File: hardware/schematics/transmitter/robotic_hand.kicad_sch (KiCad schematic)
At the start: 24 parts, among them J1 Conn_01x04_Socket, SW1 SW_BOOT, SW2 SW_RESET, U2 AMS1117-3.3, U3 ESP32-WROOM-32

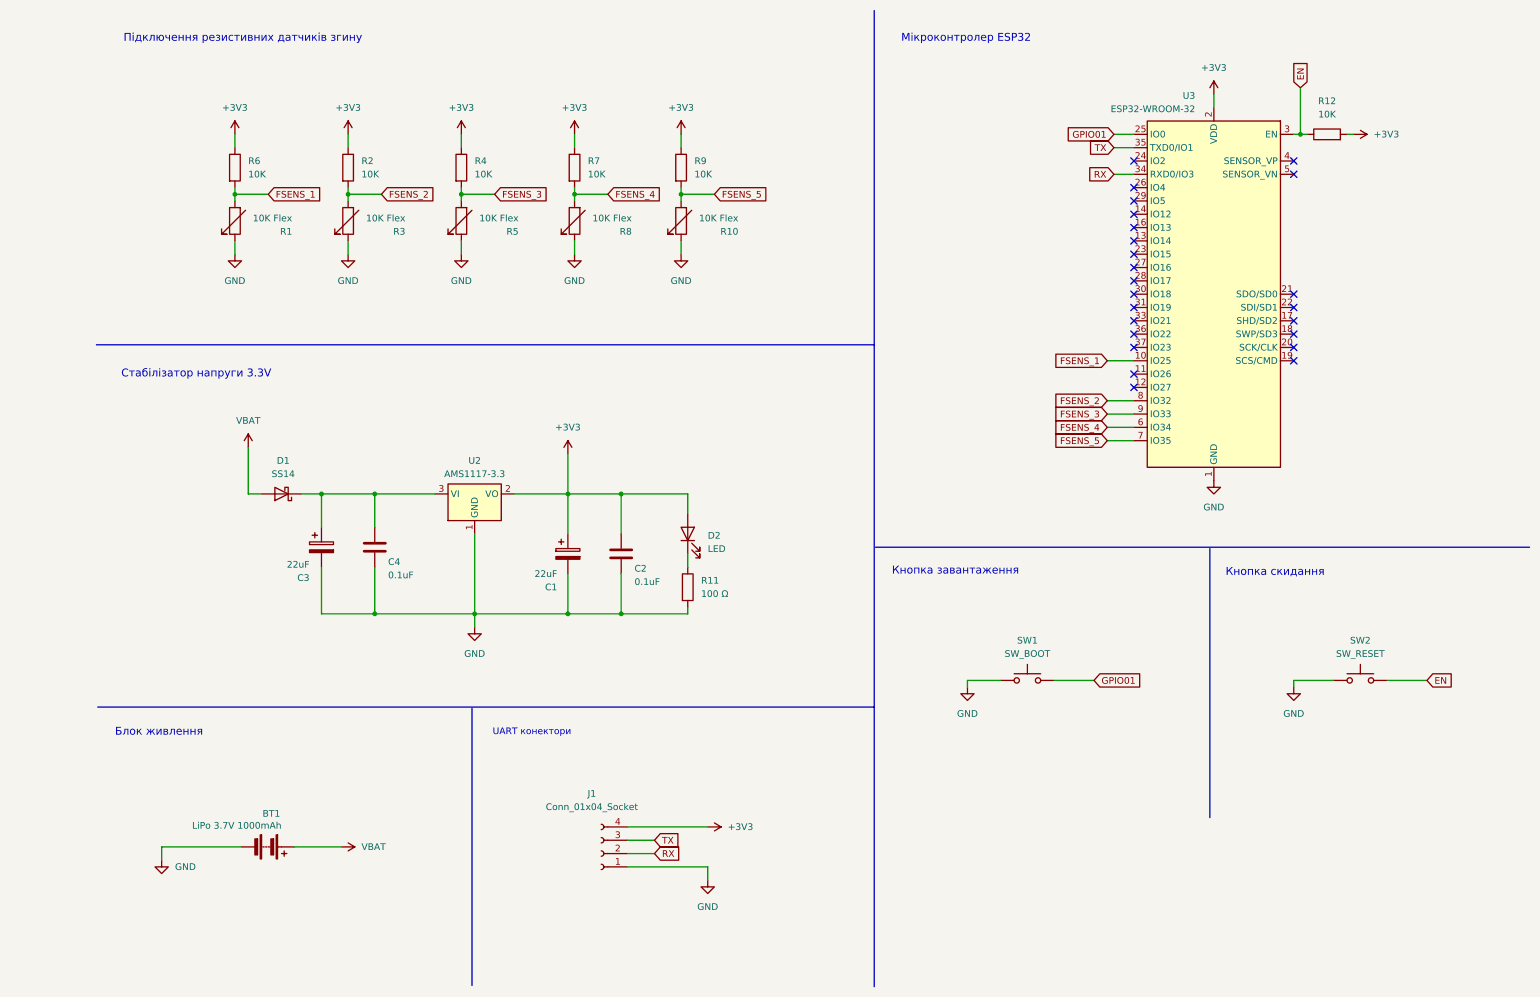
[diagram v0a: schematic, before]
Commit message: Revert schematics to rev-A Arduino design; ESP32 redesign split to separate project
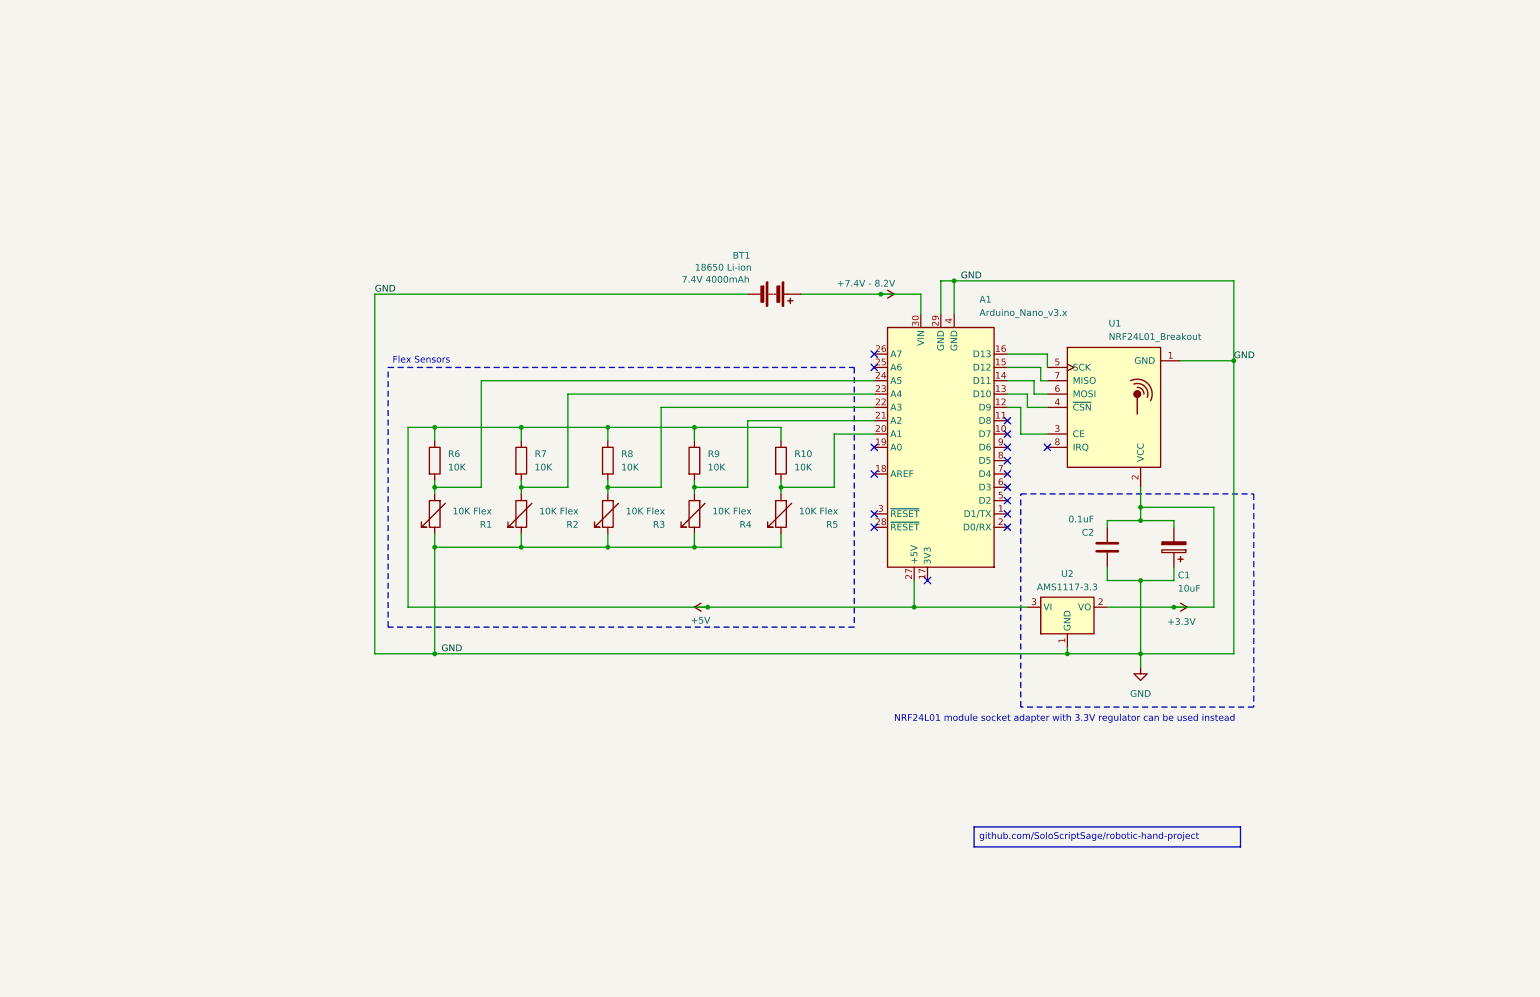
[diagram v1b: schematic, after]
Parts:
- removed C3: 22uF, Capacitor_SMD:C_1206_3216Metric, symbol Device:C_Polarized
- removed C4: 0.1uF, Capacitor_SMD:C_0805_2012Metric, symbol Device:C
- removed D1: SS14, Diode_SMD:D_SMA, symbol Diode:SS14
- removed D2: LED, LED_SMD:LED_0805_2012Metric, symbol Device:LED
- removed J1: Conn_01x04_Socket, Connector_PinHeader_2.54mm:PinHeader_1x04_P2.54mm_Vertical, symbol Connector:Conn_01x04_Socket
- removed R10, R8: 10K Flex, Connector_JST:JST_PH_S2B-PH-K_1x02_P2.00mm_Horizontal, symbol Device:R_Variable
- removed R11: 100 Ω, Resistor_SMD:R_0805_2012Metric, symbol Device:R
- removed R12, R2, R4: 10K, Resistor_SMD:R_0805_2012Metric, symbol Device:R
- removed SW1: SW_BOOT, Button_Switch_SMD:SW_SPST_B3U-1000P, symbol Switch:SW_Push
- removed SW2: SW_RESET, Button_Switch_SMD:SW_SPST_B3U-1000P, symbol Switch:SW_Push
- removed U3: ESP32-WROOM-32, RF_Module:ESP32-WROOM-32, symbol RF_Module:ESP32-WROOM-32
- added A1: Arduino_Nano_v3.x, Module:Arduino_Nano, symbol MCU_Module:Arduino_Nano_v3.x
- added R10, R8: 10K, symbol Device:R
- added R2, R4: 10K Flex, symbol Device:R_Variable
- added U1: NRF24L01_Breakout, RF_Module:nRF24L01_Breakout, symbol RF:NRF24L01_Breakout
- BT1: value LiPo 3.7V 1000mAh -> 18650 Li-ion; footprint Connector_JST:JST_PH_S2B-PH-K_1x02_P2.00mm_Horizontal -> (none)
- C1: value 22uF -> 10uF; footprint Capacitor_SMD:C_1206_3216Metric -> (none)
- C2: footprint Capacitor_SMD:C_0805_2012Metric -> (none)
- R1, R3, R5: footprint Connector_JST:JST_PH_S2B-PH-K_1x02_P2.00mm_Horizontal -> (none)
- R6, R7, R9: footprint Resistor_SMD:R_0805_2012Metric -> (none)
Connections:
- net GND: now also C1.1, C2.2, A1.29 (GND), A1.4 (GND), R2.1, R4.1, U1.1 (GND); no longer C1.2, C2.1
- net +5V: now reaches U2.3 (VI)
- net +5V: now also R6.1, R7.1, R9.1, A1.27 (+5V), R10.1, R8.1
- removed net +3V3: C1.1, C2.2, R6.1, R7.1, R9.1, U2.2 (VO)
- net FSENS_1: no longer names the net of R1.2, R6.2
- net FSENS_1: now also A1.24 (A5)
- net FSENS_2: no longer names the net of R3.2
- net FSENS_2: now also A1.22 (A3), R8.2
- net FSENS_3: no longer names the net of R5.2
- net FSENS_3: now also A1.20 (A1), R10.2
- net FSENS_4: no longer names the net of R7.2
- net FSENS_4: now also A1.23 (A4), R2.2
- net FSENS_5: no longer names the net of R9.2
- net FSENS_5: now also A1.21 (A2), R4.2
- net VBAT renamed +7.4V - 8.2V
- net +7.4V - 8.2V: now also A1.30 (VIN)
- new net: A1.12 (D9), U1.3 (CE)
- new net: A1.13 (D10), U1.4 (~{CSN})
- new net: A1.16 (D13), U1.5 (SCK)
- new net: A1.14 (D11), U1.6 (MOSI)
- new net: A1.15 (D12), U1.7 (MISO)
- new net +3.3V: C1.2, C2.1, U1.2 (VCC), U2.2 (VO)
- no-connect marks 24 -> 17
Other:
- note added: "Flex Sensors"
- note added: "NRF24L01 module socket adapter with 3.3V regulator can be used instead"
- note removed: "UART конектори"
- note removed: "Блок живлення"
- note removed: "Кнопка завантаження"
- note removed: "Кнопка скидання"
- note removed: "Мікроконтролер ESP32"
- note removed: "Підключення резистивних датчиків згину"
- note removed: "Стабілізатор напруги 3.3V"
- company: ХПФК НУ ЛП -> SoloScriptSage
- title: Додаток А: Схема електрична принципова передавача (TX)  -> Robotic Hand Transmitter
- moved on the sheet: BT1, C1, C2, R1, R6, U2

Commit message: Expand schematics and add initial PCB layouts for both boards
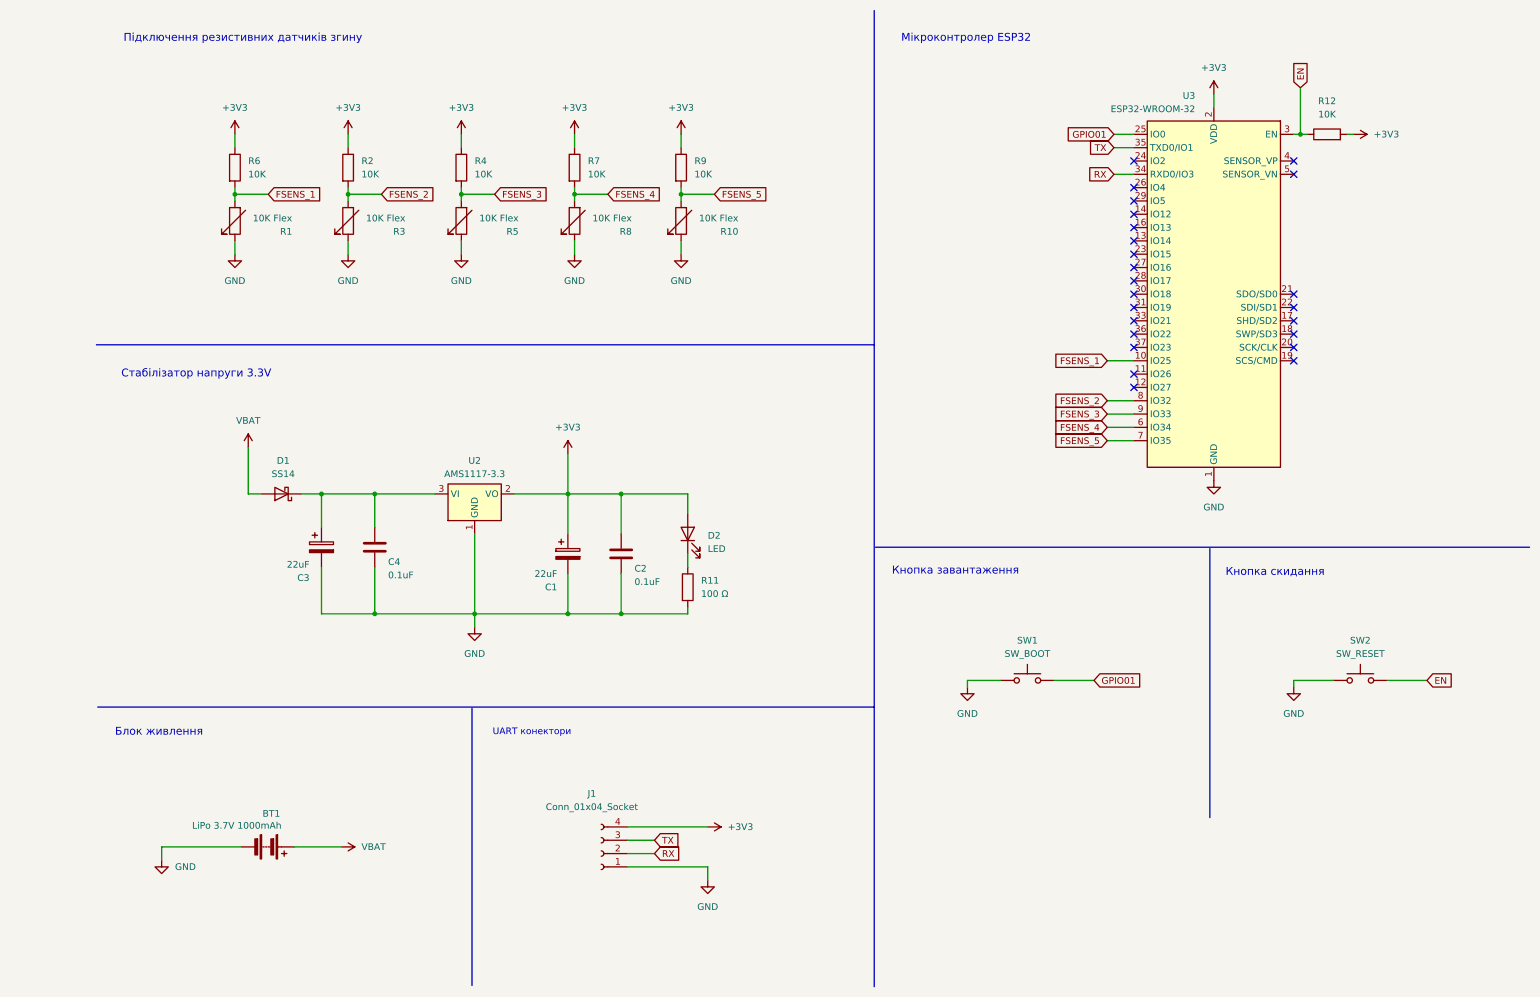
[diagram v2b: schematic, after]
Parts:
- removed A1: Arduino_Nano_v3.x, Module:Arduino_Nano, symbol MCU_Module:Arduino_Nano_v3.x
- removed R10, R8: 10K, symbol Device:R
- removed R2, R4: 10K Flex, symbol Device:R_Variable
- removed U1: NRF24L01_Breakout, RF_Module:nRF24L01_Breakout, symbol RF:NRF24L01_Breakout
- added C3: 22uF, Capacitor_SMD:C_1206_3216Metric, symbol Device:C_Polarized
- added C4: 0.1uF, Capacitor_SMD:C_0805_2012Metric, symbol Device:C
- added D1: SS14, Diode_SMD:D_SMA, symbol Diode:SS14
- added D2: LED, LED_SMD:LED_0805_2012Metric, symbol Device:LED
- added J1: Conn_01x04_Socket, Connector_PinHeader_2.54mm:PinHeader_1x04_P2.54mm_Vertical, symbol Connector:Conn_01x04_Socket
- added R10, R8: 10K Flex, Connector_JST:JST_PH_S2B-PH-K_1x02_P2.00mm_Horizontal, symbol Device:R_Variable
- added R11: 100 Ω, Resistor_SMD:R_0805_2012Metric, symbol Device:R
- added R12, R2, R4: 10K, Resistor_SMD:R_0805_2012Metric, symbol Device:R
- added SW1: SW_BOOT, Button_Switch_SMD:SW_SPST_B3U-1000P, symbol Switch:SW_Push
- added SW2: SW_RESET, Button_Switch_SMD:SW_SPST_B3U-1000P, symbol Switch:SW_Push
- added U3: ESP32-WROOM-32, RF_Module:ESP32-WROOM-32, symbol RF_Module:ESP32-WROOM-32
- BT1: value 18650 Li-ion -> LiPo 3.7V 1000mAh; footprint (none) -> Connector_JST:JST_PH_S2B-PH-K_1x02_P2.00mm_Horizontal
- C1: value 10uF -> 22uF; footprint (none) -> Capacitor_SMD:C_1206_3216Metric
- C2: footprint (none) -> Capacitor_SMD:C_0805_2012Metric
- R1, R3, R5: footprint (none) -> Connector_JST:JST_PH_S2B-PH-K_1x02_P2.00mm_Horizontal
- R6, R7, R9: footprint (none) -> Resistor_SMD:R_0805_2012Metric
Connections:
- net GND: now also C1.2, C2.1, C3.2, C4.1, J1.1 (Pin_1), R10.1, R11.2, R8.1, SW1.1, SW2.1, U3.1 (GND), U3.15 (GND), U3.38 (GND), U3.39 (GND); no longer C1.1, C2.2
- net FSENS_4: now reaches R7.2
- net FSENS_4: now also R8.2, U3.6 (IO34)
- net FSENS_5: now reaches R9.2
- net FSENS_5: now also R10.2, U3.7 (IO35)
- net FSENS_2: now reaches R3.2
- net FSENS_2: now also R2.2, U3.8 (IO32)
- net FSENS_3: now reaches R5.2
- net FSENS_3: now also R4.2, U3.9 (IO33)
- net FSENS_1: now reaches R1.2, R6.2
- net FSENS_1: now also U3.10 (IO25)
- removed net +3.3V: C1.2, C2.1, U2.2 (VO)
- net +5V renamed +3V3
- net +3V3: now also C1.1, C2.2, U2.2 (VO), D2.2 (A), J1.4 (Pin_4), R12.2, R2.1, R4.1, U3.2 (VDD); no longer U2.3 (VI)
- net +7.4V - 8.2V renamed VBAT
- net VBAT: now also D1.2 (A)
- new net: C3.1, C4.2, D1.1 (K), U2.3 (VI)
- new net: D2.1 (K), R11.1
- new net EN: R12.1, SW2.2, U3.3 (EN)
- new net GPIO01: SW1.2, U3.25 (IO0)
- new net RX: J1.2 (Pin_2), U3.34 (RXD0/IO3)
- new net TX: J1.3 (Pin_3), U3.35 (TXD0/IO1)
- no-connect marks 17 -> 24
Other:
- note added: "UART конектори"
- note added: "Блок живлення"
- note added: "Кнопка завантаження"
- note added: "Кнопка скидання"
- note added: "Мікроконтролер ESP32"
- note added: "Підключення резистивних датчиків згину"
- note added: "Стабілізатор напруги 3.3V"
- note removed: "Flex Sensors"
- note removed: "NRF24L01 module socket adapter with 3.3V regulator can be used instead"
- company: SoloScriptSage -> ХПФК НУ ЛП
- title: Robotic Hand Transmitter -> Додаток А: Схема електрична принципова передавача (TX) 
- moved on the sheet: BT1, C1, C2, R1, R6, U2
